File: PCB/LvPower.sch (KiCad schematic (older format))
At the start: 24 parts

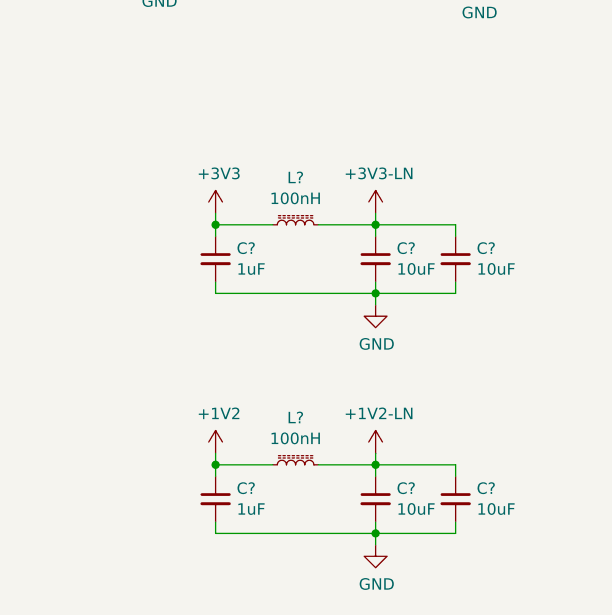
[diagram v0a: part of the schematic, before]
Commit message: Add 100m resistors to improve filter performance
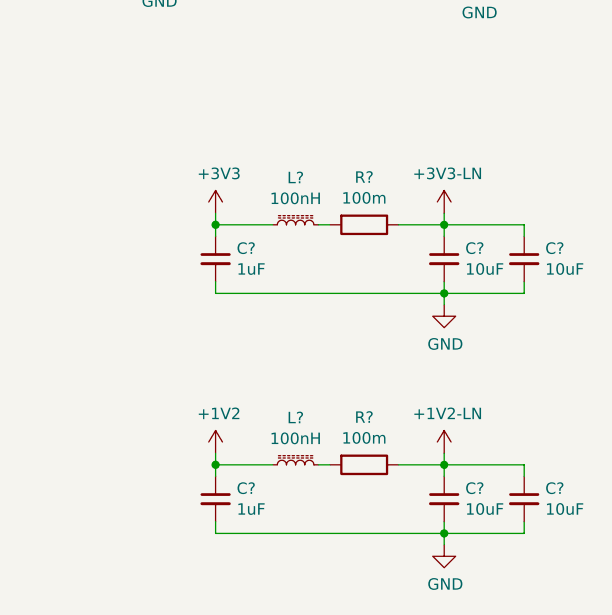
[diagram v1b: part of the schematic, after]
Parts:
- added R? (x2): 100m, Resistors_SMD:R_0805_HandSoldering, symbol Device:R
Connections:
- net +1V2-LN: now also R?.1; no longer L?.2
- net +3V3-LN: now also R?.1; no longer L?.2
- new net: L?.2, R?.2 (x2)
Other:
- moved on the sheet: C?
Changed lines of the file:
@@
 L Parts:+3V3-LN #PWR?
 U 1 1 5DD3C0A0
-P 8250 4200
-F 0 "#PWR?" H 8250 4050 50  0001 C CNN
-F 1 "+3V3-LN" H 8265 4373 50  0000 C CNN
-F 2 "" H 8250 4200 50  0001 C CNN
-F 3 "" H 8250 4200 50  0001 C CNN
-	1    8250 4200
+P 8550 4200
+F 0 "#PWR?" H 8550 4050 50  0001 C CNN
+F 1 "+3V3-LN" H 8565 4373 50  0000 C CNN
+F 2 "" H 8550 4200 50  0001 C CNN
+F 3 "" H 8550 4200 50  0001 C CNN
+	1    8550 4200
 	1    0    0    -1
 $EndComp
@@
 L Device:C_Small C?
 U 1 1 5DD3EB70
-P 8250 4400
-F 0 "C?" H 8342 4446 50  0000 L CNN
-F 1 "10uF" H 8342 4355 50  0000 L CNN
-F 2 "Capacitors_SMD:C_0805_HandSoldering" H 8250 4400 50  0001 C CNN
-F 3 "https://www.digikey.ca/product-detail/en/kemet/C0805C106K8PACTU/399-4925-1-ND/1090920" H 8250 4400 50  0001 C CNN
-	1    8250 4400
-	1    0    0    -1
-$EndComp
-Wire Wire Line
-	8250 4200 8250 4250
+P 8550 4400
+F 0 "C?" H 8642 4446 50  0000 L CNN
+F 1 "10uF" H 8642 4355 50  0000 L CNN
+F 2 "Capacitors_SMD:C_0805_HandSoldering" H 8550 4400 50  0001 C CNN
+F 3 "https://www.digikey.ca/product-detail/en/kemet/C0805C106K8PACTU/399-4925-1-ND/1090920" H 8550 4400 50  0001 C CNN
+	1    8550 4400
+	1    0    0    -1
+$EndComp
+Wire Wire Line
+	8550 4200 8550 4250
 $Comp
 L Device:C_Small C?
 U 1 1 5DD417D3
-P 8600 4400
-F 0 "C?" H 8692 4446 50  0000 L CNN
-F 1 "10uF" H 8692 4355 50  0000 L CNN
-F 2 "Capacitors_SMD:C_0805_HandSoldering" H 8600 4400 50  0001 C CNN
-F 3 "https://www.digikey.ca/product-detail/en/kemet/C0805C106K8PACTU/399-4925-1-ND/1090920" H 8600 4400 50  0001 C CNN
-	1    8600 4400
-	1    0    0    -1
-$EndComp
-Wire Wire Line
-	8250 4250 8600 4250
-Wire Wire Line
-	8600 4250 8600 4300
-Connection ~ 8250 4250
-Wire Wire Line
-	8250 4250 8250 4300
-Wire Wire Line
-	8600 4500 8600 4550
-Wire Wire Line
-	8600 4550 8250 4550
-Wire Wire Line
-	8250 4550 8250 4500
+P 8900 4400
+F 0 "C?" H 8992 4446 50  0000 L CNN
+F 1 "10uF" H 8992 4355 50  0000 L CNN
+F 2 "Capacitors_SMD:C_0805_HandSoldering" H 8900 4400 50  0001 C CNN
+F 3 "https://www.digikey.ca/product-detail/en/kemet/C0805C106K8PACTU/399-4925-1-ND/1090920" H 8900 4400 50  0001 C CNN
+	1    8900 4400
+	1    0    0    -1
+$EndComp
+Wire Wire Line
+	8550 4250 8900 4250
+Wire Wire Line
+	8900 4250 8900 4300
+Connection ~ 8550 4250
+Wire Wire Line
+	8550 4250 8550 4300
+Wire Wire Line
+	8900 4500 8900 4550
+Wire Wire Line
+	8900 4550 8550 4550
+Wire Wire Line
+	8550 4550 8550 4500
 $Comp
 L power:GND #PWR?
 U 1 1 5DD45711
-P 8250 4600
-F 0 "#PWR?" H 8250 4350 50  0001 C CNN
-F 1 "GND" H 8255 4427 50  0000 C CNN
-F 2 "" H 8250 4600 50  0001 C CNN
-F 3 "" H 8250 4600 50  0001 C CNN
-	1    8250 4600
-	1    0    0    -1
-$EndComp
-Wire Wire Line
-	8250 4600 8250 4550
-Connection ~ 8250 4550
+P 8550 4600
+F 0 "#PWR?" H 8550 4350 50  0001 C CNN
+F 1 "GND" H 8555 4427 50  0000 C CNN
+F 2 "" H 8550 4600 50  0001 C CNN
+F 3 "" H 8550 4600 50  0001 C CNN
+	1    8550 4600
+	1    0    0    -1
+$EndComp
+Wire Wire Line
+	8550 4600 8550 4550
+Connection ~ 8550 4550
 $Comp
 L Device:L_Core_Ferrite_Small L?
@@
 $EndComp
 Wire Wire Line
-	8000 4250 8250 4250
+	8350 4250 8550 4250
 Wire Wire Line
 	7800 4250 7550 4250
@@
 Wire Wire Line
 	7550 4500 7550 4550
-Wire Wire Line
-	7550 4550 8250 4550
 $Comp
 L Device:C_Small C?
 U 1 1 5DD65CDB
-P 8250 5450
-F 0 "C?" H 8342 5496 50  0000 L CNN
-F 1 "10uF" H 8342 5405 50  0000 L CNN
-F 2 "Capacitors_SMD:C_0805_HandSoldering" H 8250 5450 50  0001 C CNN
-F 3 "https://www.digikey.ca/product-detail/en/kemet/C0805C106K8PACTU/399-4925-1-ND/1090920" H 8250 5450 50  0001 C CNN
-	1    8250 5450
-	1    0    0    -1
-$EndComp
-Wire Wire Line
-	8250 5250 8250 5300
+P 8550 5450
+F 0 "C?" H 8642 5496 50  0000 L CNN
+F 1 "10uF" H 8642 5405 50  0000 L CNN
+F 2 "Capacitors_SMD:C_0805_HandSoldering" H 8550 5450 50  0001 C CNN
+F 3 "https://www.digikey.ca/product-detail/en/kemet/C0805C106K8PACTU/399-4925-1-ND/1090920" H 8550 5450 50  0001 C CNN
+	1    8550 5450
+	1    0    0    -1
+$EndComp
+Wire Wire Line
+	8550 5250 8550 5300
 $Comp
 L Device:C_Small C?
 U 1 1 5DD65CE6
-P 8600 5450
-F 0 "C?" H 8692 5496 50  0000 L CNN
-F 1 "10uF" H 8692 5405 50  0000 L CNN
-F 2 "Capacitors_SMD:C_0805_HandSoldering" H 8600 5450 50  0001 C CNN
-F 3 "https://www.digikey.ca/product-detail/en/kemet/C0805C106K8PACTU/399-4925-1-ND/1090920" H 8600 5450 50  0001 C CNN
-	1    8600 5450
-	1    0    0    -1
-$EndComp
-Wire Wire Line
-	8250 5300 8600 5300
-Wire Wire Line
-	8600 5300 8600 5350
-Connection ~ 8250 5300
-Wire Wire Line
-	8250 5300 8250 5350
-Wire Wire Line
-	8600 5550 8600 5600
-Wire Wire Line
-	8600 5600 8250 5600
-Wire Wire Line
-	8250 5600 8250 5550
+P 8900 5450
+F 0 "C?" H 8992 5496 50  0000 L CNN
+F 1 "10uF" H 8992 5405 50  0000 L CNN
+F 2 "Capacitors_SMD:C_0805_HandSoldering" H 8900 5450 50  0001 C CNN
+F 3 "https://www.digikey.ca/product-detail/en/kemet/C0805C106K8PACTU/399-4925-1-ND/1090920" H 8900 5450 50  0001 C CNN
+	1    8900 5450
+	1    0    0    -1
+$EndComp
+Wire Wire Line
+	8550 5300 8900 5300
+Wire Wire Line
+	8900 5300 8900 5350
+Connection ~ 8550 5300
+Wire Wire Line
+	8550 5300 8550 5350
+Wire Wire Line
+	8900 5550 8900 5600
+Wire Wire Line
+	8900 5600 8550 5600
+Wire Wire Line
+	8550 5600 8550 5550
 $Comp
 L power:GND #PWR?
 U 1 1 5DD65CF7
-P 8250 5650
-F 0 "#PWR?" H 8250 5400 50  0001 C CNN
-F 1 "GND" H 8255 5477 50  0000 C CNN
-F 2 "" H 8250 5650 50  0001 C CNN
-F 3 "" H 8250 5650 50  0001 C CNN
-	1    8250 5650
-	1    0    0    -1
-$EndComp
-Wire Wire Line
-	8250 5650 8250 5600
-Connection ~ 8250 5600
+P 8550 5650
+F 0 "#PWR?" H 8550 5400 50  0001 C CNN
+F 1 "GND" H 8555 5477 50  0000 C CNN
+F 2 "" H 8550 5650 50  0001 C CNN
+F 3 "" H 8550 5650 50  0001 C CNN
+	1    8550 5650
+	1    0    0    -1
+$EndComp
+Wire Wire Line
+	8550 5650 8550 5600
+Connection ~ 8550 5600
 $Comp
 L Device:L_Core_Ferrite_Small L?
@@
 $EndComp
 Wire Wire Line
-	8000 5300 8250 5300
+	8350 5300 8550 5300
 Wire Wire Line
 	7800 5300 7550 5300
@@
 Wire Wire Line
 	7550 5550 7550 5600
-Wire Wire Line
-	7550 5600 8250 5600
 $Comp
 L power:+1V2 #PWR?
@@
 L Parts:+1V2-LN #PWR?
 U 1 1 5DD6F7D4
-P 8250 5250
-F 0 "#PWR?" H 8250 5100 50  0001 C CNN
-F 1 "+1V2-LN" H 8265 5423 50  0000 C CNN
-F 2 "" H 8250 5250 50  0001 C CNN
-F 3 "" H 8250 5250 50  0001 C CNN
-	1    8250 5250
-	1    0    0    -1
-$EndComp
+P 8550 5250
+F 0 "#PWR?" H 8550 5100 50  0001 C CNN
+F 1 "+1V2-LN" H 8565 5423 50  0000 C CNN
+F 2 "" H 8550 5250 50  0001 C CNN
+F 3 "" H 8550 5250 50  0001 C CNN
+	1    8550 5250
+	1    0    0    -1
+$EndComp
+$Comp
+L Device:R R?
+U 1 1 5DDCE692
+P 8200 4250
+F 0 "R?" V 7993 4250 50  0000 C CNN
+F 1 "100m" V 8084 4250 50  0000 C CNN
+F 2 "Resistors_SMD:R_0805_HandSoldering" V 8130 4250 50  0001 C CNN
+F 3 "https://www.digikey.ca/product-detail/en/cts-resistor-products/73L3R10J/73L3R10JCT-ND/1543529" H 8200 4250 50  0001 C CNN
+	1    8200 4250
+	0    1    1    0
+$EndComp
+Wire Wire Line
+	8000 4250 8050 4250
+Wire Wire Line
+	7550 4550 8550 4550
+$Comp
+L Device:R R?
+U 1 1 5DDED10A
+P 8200 5300
+F 0 "R?" V 7993 5300 50  0000 C CNN
+F 1 "100m" V 8084 5300 50  0000 C CNN
+F 2 "Resistors_SMD:R_0805_HandSoldering" V 8130 5300 50  0001 C CNN
+F 3 "https://www.digikey.ca/product-detail/en/cts-resistor-products/73L3R10J/73L3R10JCT-ND/1543529" H 8200 5300 50  0001 C CNN
+	1    8200 5300
+	0    1    1    0
+$EndComp
+Wire Wire Line
+	8000 5300 8050 5300
+Wire Wire Line
+	7550 5600 8550 5600
 $EndSCHEMATC

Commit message: Added soldered jumpers to LV power schematic
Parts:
- added JP? (x4): 0, Parts:SolderJumper_0603, symbol Jumper:SolderJumper_2_Bridged
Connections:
- net +1V2: now also JP?.2 (B); no longer L?.2, U?.3 (FB)
- net +3V3: now also JP?.2 (B); no longer U?.1 (VOUT), U?.10 (FB)
- net +BATT: now also JP?.1 (A), JP?.1 (A); no longer C?.1, C?.1, U?.2 (MODE), U?.4 (EN), U?.5 (VIN), U?.5 (VIN)
- new net: C?.1, JP?.2 (B), U?.5 (VIN)
- new net: C?.1, JP?.2 (B), U?.2 (MODE), U?.4 (EN), U?.5 (VIN)
- new net: JP?.1 (A), L?.2, U?.3 (FB)
- new net: JP?.1 (A), U?.1 (VOUT), U?.10 (FB)
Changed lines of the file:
@@
 Connection ~ 2600 2500
 Wire Wire Line
-	2600 2450 2600 2500
+	2600 2100 2600 2150
 Wire Wire Line
 	4150 3350 4250 3350
@@
 L power:+BATT #PWR0103
 U 1 1 5DCDADE4
-P 2600 2450
-F 0 "#PWR0103" H 2600 2300 50  0001 C CNN
-F 1 "+BATT" H 2615 2623 50  0000 C CNN
-F 2 "" H 2600 2450 50  0001 C CNN
-F 3 "" H 2600 2450 50  0001 C CNN
-	1    2600 2450
+P 2600 2100
+F 0 "#PWR0103" H 2600 1950 50  0001 C CNN
+F 1 "+BATT" H 2615 2273 50  0000 C CNN
+F 2 "" H 2600 2100 50  0001 C CNN
+F 3 "" H 2600 2100 50  0001 C CNN
+	1    2600 2100
 	1    0    0    -1
 $EndComp
@@
 L power:+BATT #PWR0105
 U 1 1 5DD163FB
-P 3150 4700
-F 0 "#PWR0105" H 3150 4550 50  0001 C CNN
-F 1 "+BATT" H 3165 4873 50  0000 C CNN
-F 2 "" H 3150 4700 50  0001 C CNN
-F 3 "" H 3150 4700 50  0001 C CNN
-	1    3150 4700
+P 3150 4350
+F 0 "#PWR0105" H 3150 4200 50  0001 C CNN
+F 1 "+BATT" H 3165 4523 50  0000 C CNN
+F 2 "" H 3150 4350 50  0001 C CNN
+F 3 "" H 3150 4350 50  0001 C CNN
+	1    3150 4350
 	1    0    0    -1
 $EndComp
@@
 Connection ~ 3600 4850
 Wire Wire Line
-	3150 4700 3150 4750
+	3150 4350 3150 4400
 Wire Wire Line
 	3150 4750 3600 4750
@@
 	4500 4750 4450 4750
 Wire Wire Line
-	4750 4750 5300 4750
+	4750 4750 4950 4750
 Connection ~ 4750 4750
 $Comp
@@
 	4550 2600 4550 2500
 Wire Wire Line
-	4550 2500 5300 2500
+	4550 2500 4950 2500
 Connection ~ 4550 2500
 $Comp
@@
 Wire Wire Line
 	7550 5600 8550 5600
+$Comp
+L Jumper:SolderJumper_2_Bridged JP?
+U 1 1 5DE955D5
+P 5100 4750
+F 0 "JP?" H 5100 4955 50  0000 C CNN
+F 1 "0" H 5100 4864 50  0000 C CNN
+F 2 "Parts:SolderJumper_0603" H 5100 4750 50  0001 C CNN
+F 3 "" H 5100 4750 50  0001 C CNN
+	1    5100 4750
+	1    0    0    -1
+$EndComp
+$Comp
+L Jumper:SolderJumper_2_Bridged JP?
+U 1 1 5DE9B086
+P 2600 2300
+F 0 "JP?" V 2554 2368 50  0000 L CNN
+F 1 "0" V 2645 2368 50  0000 L CNN
+F 2 "Parts:SolderJumper_0603" H 2600 2300 50  0001 C CNN
+F 3 "" H 2600 2300 50  0001 C CNN
+	1    2600 2300
+	0    1    1    0
+$EndComp
+Wire Wire Line
+	2600 2450 2600 2500
+$Comp
+L Jumper:SolderJumper_2_Bridged JP?
+U 1 1 5DEA0F33
+P 5100 2500
+F 0 "JP?" H 5100 2705 50  0000 C CNN
+F 1 "0" H 5100 2614 50  0000 C CNN
+F 2 "Parts:SolderJumper_0603" H 5100 2500 50  0001 C CNN
+F 3 "" H 5100 2500 50  0001 C CNN
+	1    5100 2500
+	1    0    0    -1
+$EndComp
+Wire Wire Line
+	5250 2500 5300 2500
+$Comp
+L Jumper:SolderJumper_2_Bridged JP?
+U 1 1 5DEA5A0E
+P 3150 4550
+F 0 "JP?" V 3104 4618 50  0000 L CNN
+F 1 "0" V 3195 4618 50  0000 L CNN
+F 2 "Parts:SolderJumper_0603" H 3150 4550 50  0001 C CNN
+F 3 "" H 3150 4550 50  0001 C CNN
+	1    3150 4550
+	0    1    1    0
+$EndComp
+Wire Wire Line
+	3150 4700 3150 4750
+Wire Wire Line
+	5250 4750 5300 4750
 $EndSCHEMATC

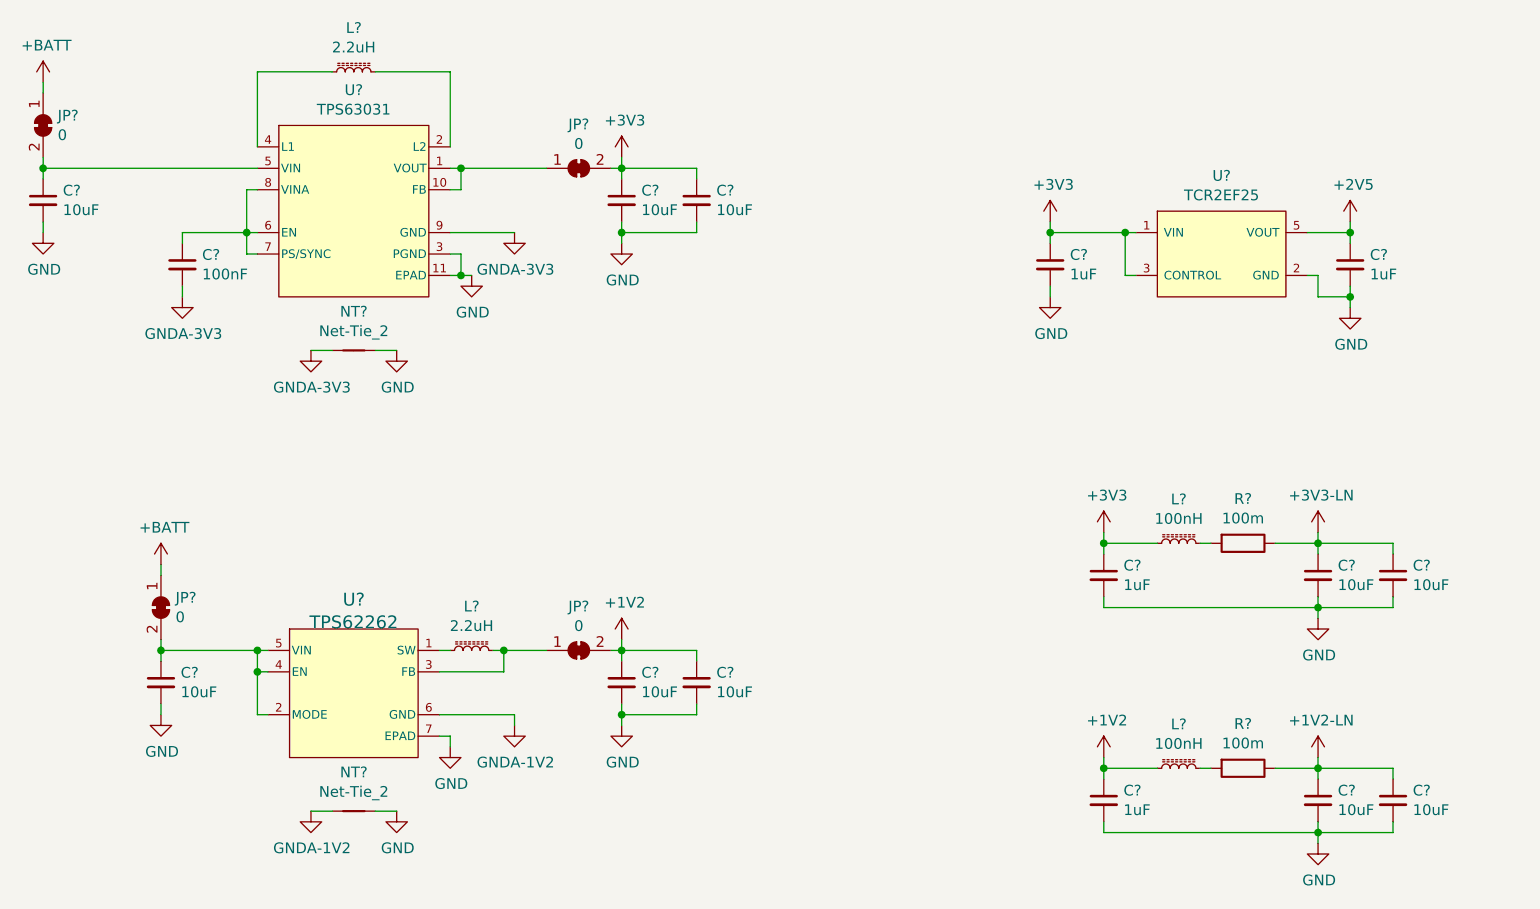
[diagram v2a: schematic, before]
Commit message: Add decoupling and bulk capacitance for FPGA
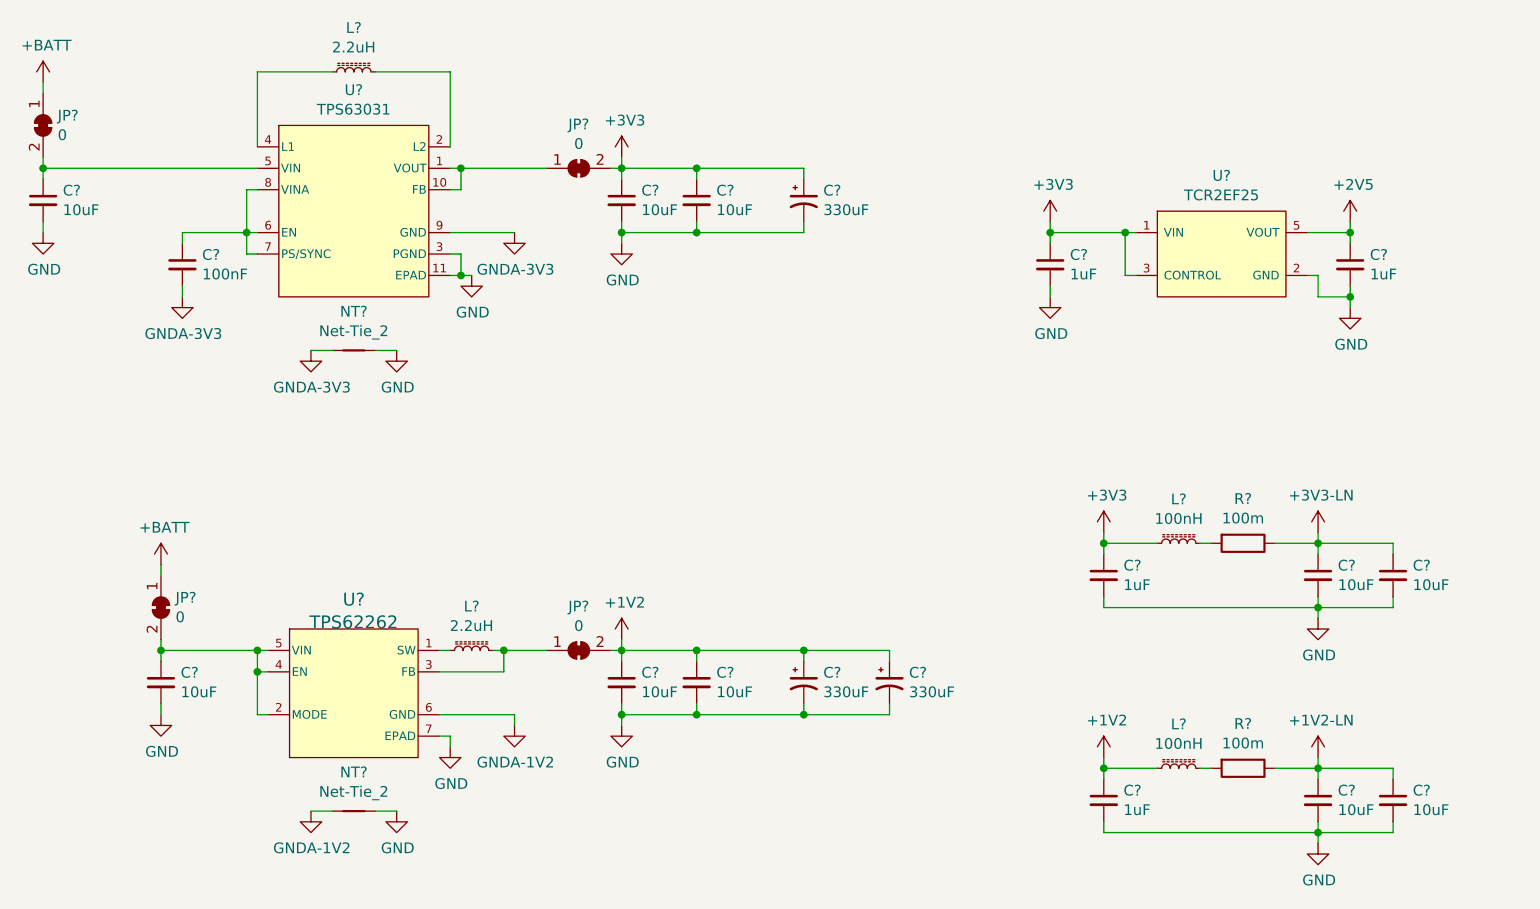
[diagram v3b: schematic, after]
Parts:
- added C? (x3): 330uF, Capacitors_THT:CP_Radial_D6.3mm_P2.50mm, symbol Device:CP1_Small
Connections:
- net +1V2: now also C?.1, C?.1
- net +3V3: now also C?.1
- net GND: now also C?.2, C?.2, C?.2
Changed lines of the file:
@@
 Wire Wire Line
 	5250 4750 5300 4750
+$Comp
+L Device:CP1_Small C?
+U 1 1 5DFB66E6
+P 6150 2650
+F 0 "C?" H 6241 2696 50  0000 L CNN
+F 1 "330uF" H 6241 2605 50  0000 L CNN
+F 2 "Capacitors_THT:CP_Radial_D6.3mm_P2.50mm" H 6150 2650 50  0001 C CNN
+F 3 "https://www.digikey.ca/product-detail/en/w-rth-elektronik/860020273010/732-8912-1-ND/5728855" H 6150 2650 50  0001 C CNN
+	1    6150 2650
+	1    0    0    -1
+$EndComp
+Wire Wire Line
+	5650 2500 6150 2500
+Wire Wire Line
+	6150 2500 6150 2550
+Connection ~ 5650 2500
+Wire Wire Line
+	6150 2750 6150 2800
+Wire Wire Line
+	6150 2800 5650 2800
+Connection ~ 5650 2800
+$Comp
+L Device:CP1_Small C?
+U 1 1 5DFBFE57
+P 6150 4900
+F 0 "C?" H 6241 4946 50  0000 L CNN
+F 1 "330uF" H 6241 4855 50  0000 L CNN
+F 2 "Capacitors_THT:CP_Radial_D6.3mm_P2.50mm" H 6150 4900 50  0001 C CNN
+F 3 "https://www.digikey.ca/product-detail/en/w-rth-elektronik/860020273010/732-8912-1-ND/5728855" H 6150 4900 50  0001 C CNN
+	1    6150 4900
+	1    0    0    -1
+$EndComp
+$Comp
+L Device:CP1_Small C?
+U 1 1 5DFC0807
+P 6550 4900
+F 0 "C?" H 6641 4946 50  0000 L CNN
+F 1 "330uF" H 6641 4855 50  0000 L CNN
+F 2 "Capacitors_THT:CP_Radial_D6.3mm_P2.50mm" H 6550 4900 50  0001 C CNN
+F 3 "https://www.digikey.ca/product-detail/en/w-rth-elektronik/860020273010/732-8912-1-ND/5728855" H 6550 4900 50  0001 C CNN
+	1    6550 4900
+	1    0    0    -1
+$EndComp
+Wire Wire Line
+	5650 4750 6150 4750
+Wire Wire Line
+	6150 4750 6150 4800
+Connection ~ 5650 4750
+Wire Wire Line
+	6150 4750 6550 4750
+Wire Wire Line
+	6550 4750 6550 4800
+Connection ~ 6150 4750
+Wire Wire Line
+	5650 5050 6150 5050
+Wire Wire Line
+	6150 5050 6150 5000
+Connection ~ 5650 5050
+Wire Wire Line
+	6150 5050 6550 5050
+Wire Wire Line
+	6550 5050 6550 5000
+Connection ~ 6150 5050
 $EndSCHEMATC

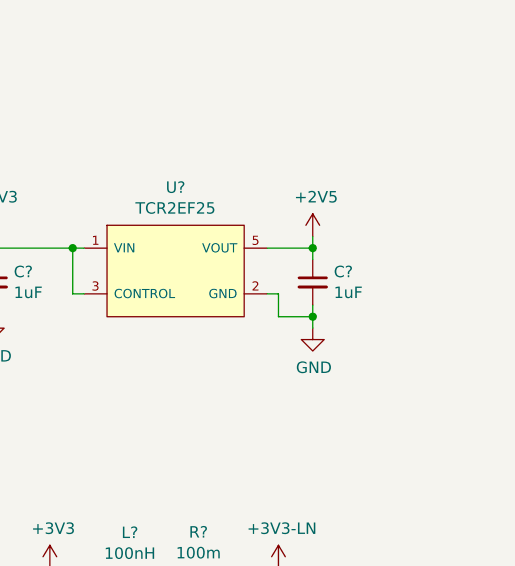
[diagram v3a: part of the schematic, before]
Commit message: Add decoupling for other FPGA supplies
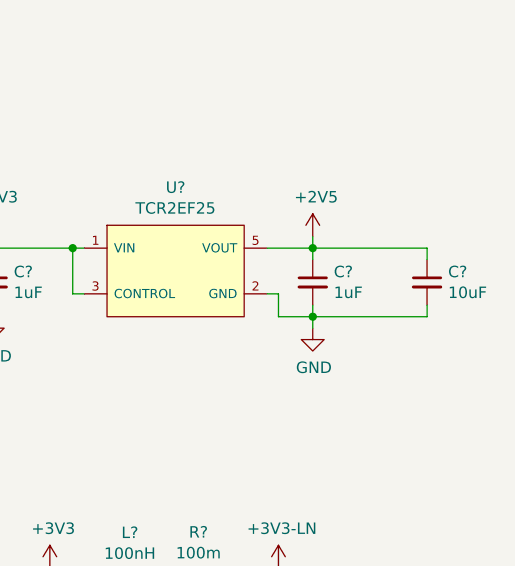
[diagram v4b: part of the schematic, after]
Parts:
- added C?: 10uF, Capacitors_SMD:C_0805_HandSoldering, symbol Device:C_Small
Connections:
- net +2V5: now also C?.1
- net GND: now also C?.2
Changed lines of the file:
@@
 	6550 5050 6550 5000
 Connection ~ 6150 5050
+$Comp
+L Device:C_Small C?
+U 1 1 5DFDFA9E
+P 9200 2950
+F 0 "C?" H 9292 2996 50  0000 L CNN
+F 1 "10uF" H 9292 2905 50  0000 L CNN
+F 2 "Capacitors_SMD:C_0805_HandSoldering" H 9200 2950 50  0001 C CNN
+F 3 "https://www.digikey.ca/product-detail/en/kemet/C0805C106K8PACTU/399-4925-1-ND/1090920" H 9200 2950 50  0001 C CNN
+	1    9200 2950
+	1    0    0    -1
+$EndComp
+Wire Wire Line
+	8700 2800 9200 2800
+Wire Wire Line
+	9200 2800 9200 2850
+Wire Wire Line
+	8700 3100 9200 3100
+Wire Wire Line
+	9200 3100 9200 3050
 $EndSCHEMATC
